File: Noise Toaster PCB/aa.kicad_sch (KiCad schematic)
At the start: 11 parts, among them J9 Amp, U3 LM386

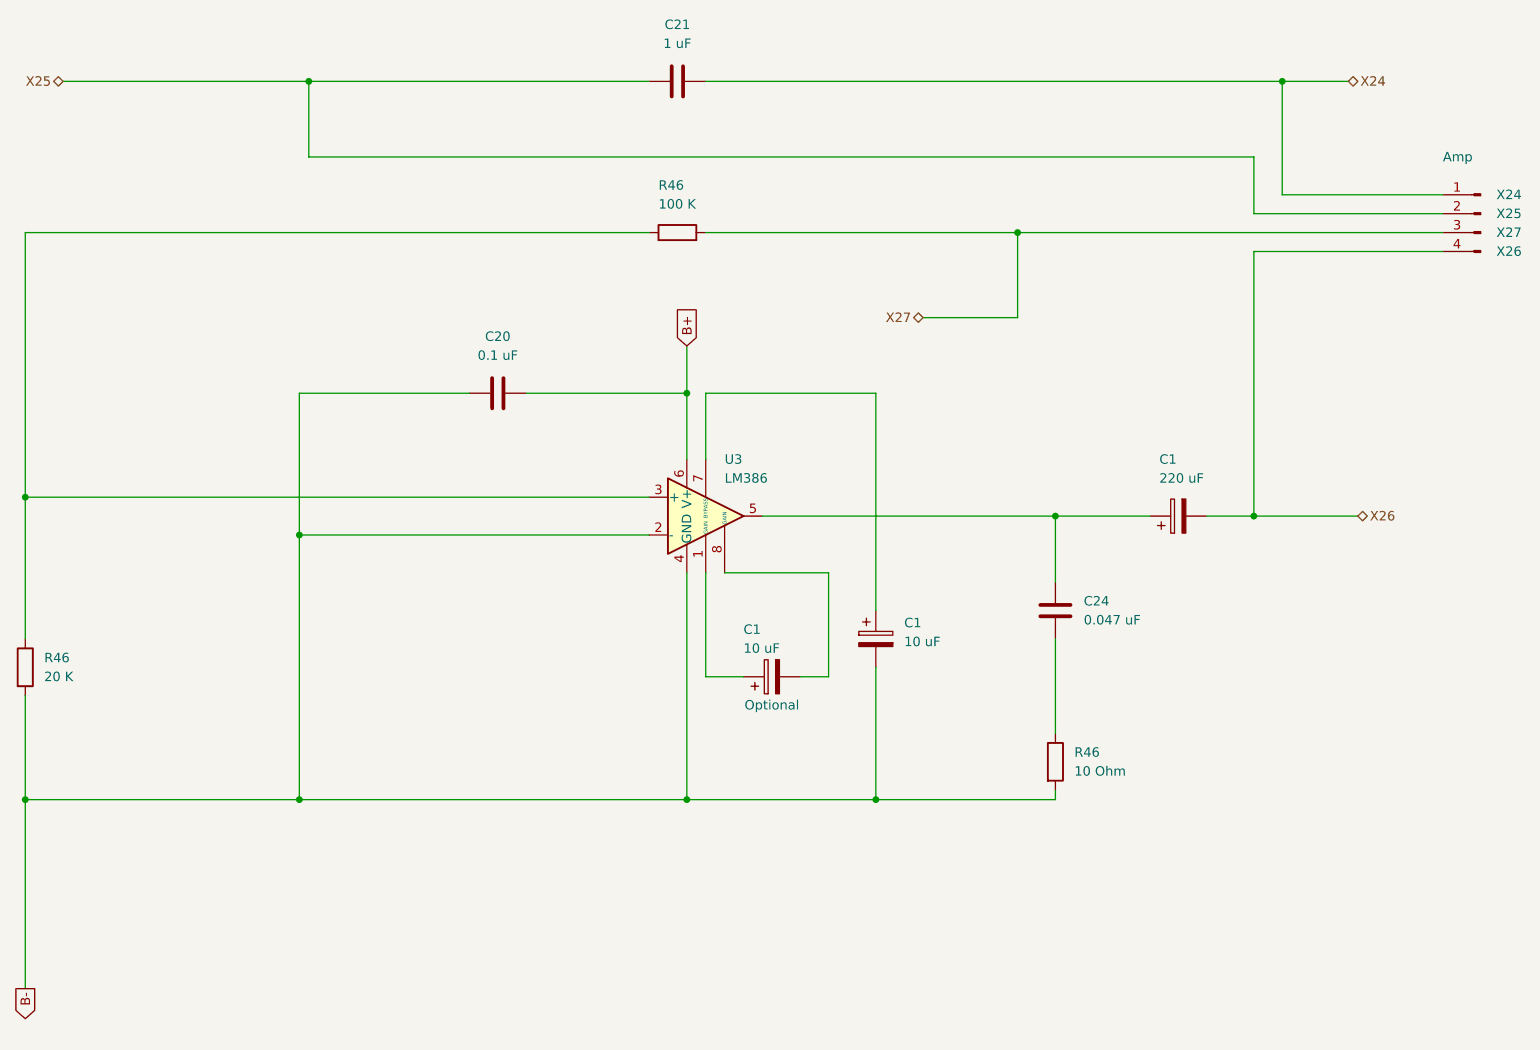
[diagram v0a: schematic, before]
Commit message: added front panel pcb
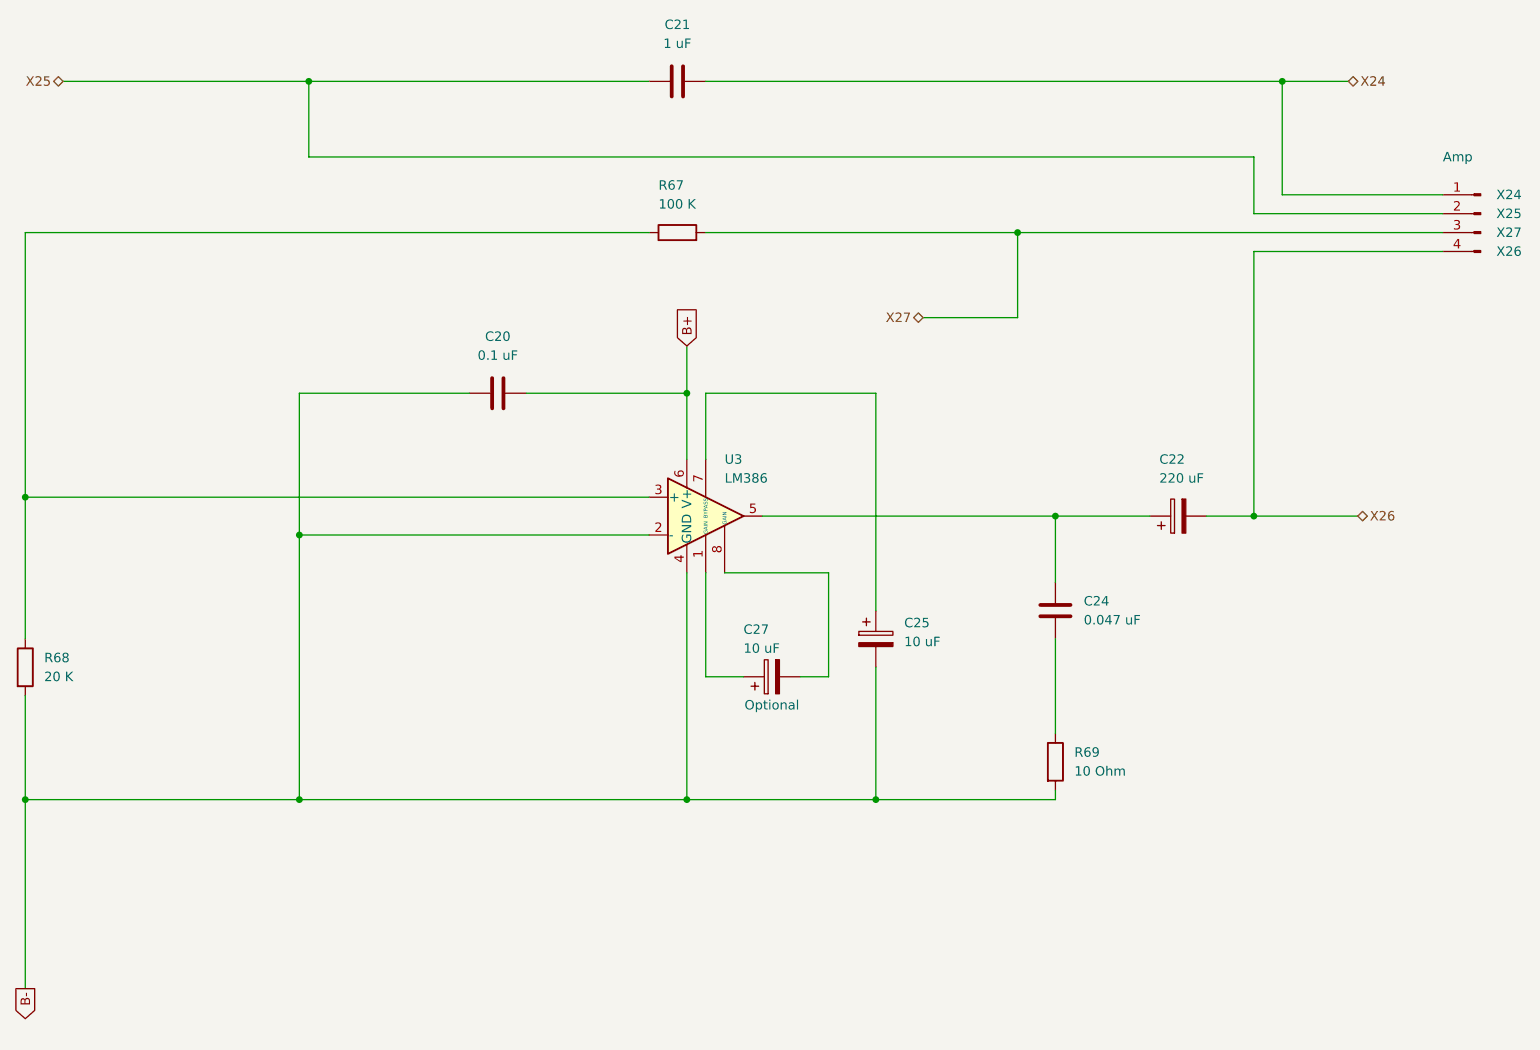
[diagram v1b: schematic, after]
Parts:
- renumbered C1 to C22, C1 to C25, C1 to C27, R46 to R67, R46 to R68, R46 to R69
